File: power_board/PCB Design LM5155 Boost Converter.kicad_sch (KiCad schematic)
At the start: 62 parts, among them Q1 BSC035N04LS G, U1 LM5155_DSSR

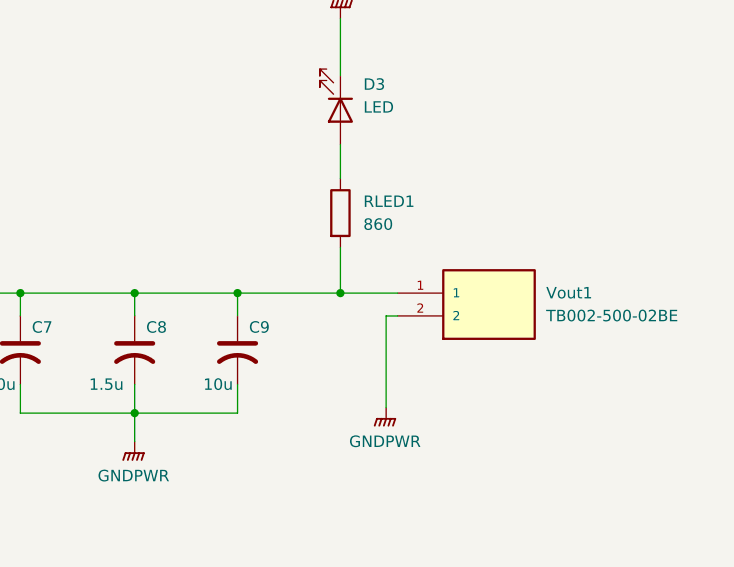
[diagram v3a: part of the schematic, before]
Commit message: Routing for TPS Module
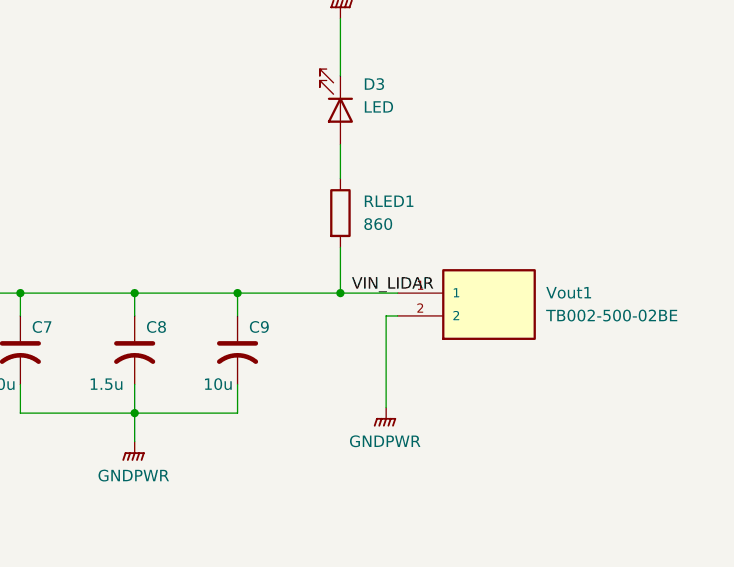
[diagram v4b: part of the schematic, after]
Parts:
- C18, C19, C21, C29: footprint (none) -> Capacitor_SMD:C_0805_2012Metric_Pad1.18x1.45mm_HandSolder
- C20, C28: footprint (none) -> Capacitor_SMD:C_1206_3216Metric_Pad1.33x1.80mm_HandSolder
- C22, C23, C30: footprint (none) -> Capacitor_SMD:C_0402_1005Metric_Pad0.74x0.62mm_HandSolder
- C24, C25: footprint (none) -> Capacitor_SMD:C_0201_0603Metric_Pad0.64x0.40mm_HandSolder
- C26, C27: footprint (none) -> Capacitor_SMD:C_0603_1608Metric_Pad1.08x0.95mm_HandSolder
- D4: footprint (none) -> Diode_SMD:D_SOD-123
- D5: footprint (none) -> LED_SMD:LED_0805_2012Metric_Pad1.15x1.40mm_HandSolder
- L2: footprint (none) -> Inductor_SMD:L_Vishay_IHLP-4040
- R10, R15, R9: footprint (none) -> Resistor_SMD:R_0603_1608Metric_Pad0.98x0.95mm_HandSolder
- R11, R12, R13, R14, R16, R17, R18, R19: footprint (none) -> Resistor_SMD:R_0402_1005Metric_Pad0.72x0.64mm_HandSolder
- TPS1: footprint (none) -> TPS552892RYQR:CONV_TPS552892RYQR
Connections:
- net VIN_LIDAR is gone; now on net COUT: C18.1, C19.1, C20.1, R18.1, TPS1.7 (VIN)
- net GND: no longer C18.2
- net PGND: now also C18.2
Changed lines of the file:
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@@
 		)
 	)
+	(label "VIN_LIDAR"
+		(at 427.99 49.53 0)
+		(effects
+			(font
+				(size 1.27 1.27)
+			)
+			(justify left bottom)
+		)
+	)
 	(label "RSENSE"
 		(at 228.6 129.54 0)
@@
 			)
 		)
-		(property "Footprint" ""
+		(property "Footprint" "Resistor_SMD:R_0402_1005Metric_Pad0.72x0.64mm_HandSolder"
 			(at 168.91 231.648 90)
 			(hide yes)
@@
 			)
 		)
-		(property "Footprint" ""
+		(property "Footprint" "Capacitor_SMD:C_0805_2012Metric_Pad1.18x1.45mm_HandSolder"
 			(at 104.14 240.3348 0)
 			(hide yes)
@@
 			)
 		)
-		(property "Footprint" ""
+		(property "Footprint" "Capacitor_SMD:C_0402_1005Metric_Pad0.74x0.62mm_HandSolder"
 			(at 143.2052 227.33 0)
 			(hide yes)
@@
 			)
 		)
-		(property "Footprint" ""
+		(property "Footprint" "Inductor_SMD:L_Vishay_IHLP-4040"
 			(at 134.62 213.36 0)
 			(hide yes)
@@
 			)
 		)
-		(property "Footprint" ""
+		(property "Footprint" "Resistor_SMD:R_0402_1005Metric_Pad0.72x0.64mm_HandSolder"
 			(at 174.752 262.89 90)
 			(hide yes)
@@
 	)
 	(symbol
-		(lib_id "power:GNDPWR")
-		(at 91.44 243.84 0)
-		(unit 1)
-		(body_style 1)
-		(exclude_from_sim no)
-		(in_bom yes)
-		(on_board yes)
-		(in_pos_files yes)
-		(dnp no)
-		(fields_autoplaced yes)
-		(property "Reference" "#PWR019"
-			(at 91.44 248.92 0)
-			(hide yes)
-			(show_name no)
-			(do_not_autoplace no)
-			(effects
-				(font
-					(size 1.27 1.27)
-				)
-			)
-		)
-		(property "Value" "GNDPWR"
-			(at 91.313 247.65 0)
-			(hide yes)
-			(show_name no)
-			(do_not_autoplace no)
-			(effects
-				(font
-					(size 1.27 1.27)
-				)
-			)
-		)
-		(property "Footprint" ""
-			(at 91.44 245.11 0)
-			(hide yes)
-			(show_name no)
-			(do_not_autoplace no)
-			(effects
-				(font
-					(size 1.27 1.27)
-				)
-			)
-		)
-		(property "Datasheet" ""
-			(at 91.44 245.11 0)
-			(hide yes)
-			(show_name no)
-			(do_not_autoplace no)
-			(effects
-				(font
-					(size 1.27 1.27)
-				)
-			)
-		)
-		(property "Description" "Power symbol creates a global label with name \"GNDPWR\" , global ground"
-			(at 91.44 243.84 0)
-			(hide yes)
-			(show_name no)
-			(do_not_autoplace no)
-			(effects
-				(font
-					(size 1.27 1.27)
-				)
-			)
-		)
-		(pin "1"
-		)
-		(instances
-			(project "PCB Design LM5155 Boost Converter"
-				(path "/085c1d8f-d12d-46a1-b7b5-945f7ea1ec15"
-					(reference "#PWR019")
-					(unit 1)
-				)
-			)
-		)
-	)
-	(symbol
 		(lib_id "power:GND")
 		(at 300.99 93.98 0)
@@
 			)
 		)
-		(property "Footprint" ""
+		(property "Footprint" "Capacitor_SMD:C_0603_1608Metric_Pad1.08x0.95mm_HandSolder"
 			(at 177.4952 274.32 0)
 			(hide yes)
@@
 			)
 		)
-		(property "Footprint" ""
+		(property "Footprint" "Capacitor_SMD:C_0805_2012Metric_Pad1.18x1.45mm_HandSolder"
 			(at 164.7952 243.84 0)
 			(hide yes)
@@
 			)
 		)
-		(property "Footprint" ""
+		(property "Footprint" "Capacitor_SMD:C_0201_0603Metric_Pad0.64x0.40mm_HandSolder"
 			(at 97.4852 262.89 0)
 			(hide yes)
@@
 			)
 		)
-		(property "Footprint" ""
+		(property "Footprint" "Capacitor_SMD:C_0805_2012Metric_Pad1.18x1.45mm_HandSolder"
 			(at 84.7852 243.84 0)
 			(hide yes)
@@
 			)
 		)
-		(property "Footprint" ""
+		(property "Footprint" "Capacitor_SMD:C_0402_1005Metric_Pad0.74x0.62mm_HandSolder"
 			(at 127.9652 227.33 0)
 			(hide yes)
@@
 			)
 		)
-		(property "Footprint" ""
+		(property "Footprint" "Resistor_SMD:R_0603_1608Metric_Pad0.98x0.95mm_HandSolder"
 			(at 187.452 243.84 90)
 			(hide yes)
@@
 			)
 		)
-		(property "Footprint" ""
+		(property "Footprint" "Capacitor_SMD:C_0402_1005Metric_Pad0.74x0.62mm_HandSolder"
 			(at 180.34 246.6848 0)
 			(hide yes)
@@
 			)
 		)
-		(property "Footprint" ""
+		(property "Footprint" "LED_SMD:LED_0805_2012Metric_Pad1.15x1.40mm_HandSolder"
 			(at 176.53 229.87 0)
 			(hide yes)
@@
 			)
 		)
-		(property "Footprint" ""
+		(property "Footprint" "Capacitor_SMD:C_1206_3216Metric_Pad1.33x1.80mm_HandSolder"
 			(at 77.1652 243.84 0)
 			(hide yes)
@@
 			)
 		)
-		(property "Footprint" ""
+		(property "Footprint" "Resistor_SMD:R_0402_1005Metric_Pad0.72x0.64mm_HandSolder"
 			(at 103.632 260.35 90)
 			(hide yes)
@@
 			)
 		)
-		(property "Footprint" ""
+		(property "Footprint" "Diode_SMD:D_SOD-123"
 			(at 68.58 257.81 0)
 			(hide yes)
@@
 			)
 		)
-		(property "Footprint" ""
+		(property "Footprint" "Resistor_SMD:R_0402_1005Metric_Pad0.72x0.64mm_HandSolder"
 			(at 198.882 243.84 90)
 			(hide yes)
@@
 			)
 		)
-		(property "Footprint" ""
+		(property "Footprint" "Resistor_SMD:R_0402_1005Metric_Pad0.72x0.64mm_HandSolder"
 			(at 153.162 269.24 90)
 			(hide yes)
@@
 			)
 		)
-		(property "Footprint" ""
+		(property "Footprint" "TPS552892RYQR:CONV_TPS552892RYQR"
 			(at 119.38 236.22 0)
 			(hide yes)
@@
 			)
 		)
-		(property "Footprint" ""
+		(property "Footprint" "Resistor_SMD:R_0402_1005Metric_Pad0.72x0.64mm_HandSolder"
 			(at 66.802 243.84 90)
 			(hide yes)
@@
 			)
 		)
-		(property "Footprint" ""
+		(property "Footprint" "Capacitor_SMD:C_1206_3216Metric_Pad1.33x1.80mm_HandSolder"
 			(at 158.4452 243.84 0)
 			(hide yes)
@@
 			)
 		)
-		(property "Footprint" ""
+		(property "Footprint" "Resistor_SMD:R_0402_1005Metric_Pad0.72x0.64mm_HandSolder"
 			(at 176.53 237.998 90)
 			(hide yes)
@@
 			)
 		)
-		(property "Footprint" ""
+		(property "Footprint" "Resistor_SMD:R_0603_1608Metric_Pad0.98x0.95mm_HandSolder"
 			(at 110.49 248.158 90)
 			(hide yes)
@@
 			)
 		)
-		(property "Footprint" ""
+		(property "Footprint" "Resistor_SMD:R_0402_1005Metric_Pad0.72x0.64mm_HandSolder"
 			(at 187.452 262.89 90)
 			(hide yes)
@@
 	)
 	(symbol
+		(lib_id "power:GNDPWR")
+		(at 91.44 243.84 0)
+		(unit 1)
+		(body_style 1)
+		(exclude_from_sim no)
+		(in_bom yes)
+		(on_board yes)
+		(in_pos_files yes)
+		(dnp no)
+		(fields_autoplaced yes)
+		(property "Reference" "#PWR019"
+			(at 91.44 248.92 0)
+			(hide yes)
+			(show_name no)
+			(do_not_autoplace no)
+			(effects
+				(font
+					(size 1.27 1.27)
+				)
+			)
+		)
+		(property "Value" "PGND"
+			(at 91.313 247.65 0)
+			(hide yes)
+			(show_name no)
+			(do_not_autoplace no)
+			(effects
+				(font
+					(size 1.27 1.27)
+				)
+			)
+		)
+		(property "Footprint" ""
+			(at 91.44 245.11 0)
+			(hide yes)
+			(show_name no)
+			(do_not_autoplace no)
+			(effects
+				(font
+					(size 1.27 1.27)
+				)
+			)
+		)
+		(property "Datasheet" ""
+			(at 91.44 245.11 0)
+			(hide yes)
+			(show_name no)
+			(do_not_autoplace no)
+			(effects
+				(font
+					(size 1.27 1.27)
+				)
+			)
+		)
+		(property "Description" "Power symbol creates a global label with name \"GNDPWR\" , global ground"
+			(at 91.44 243.84 0)
+			(hide yes)
+			(show_name no)
+			(do_not_autoplace no)
+			(effects
+				(font
+					(size 1.27 1.27)
+				)
+			)
+		)
+		(pin "1"
+		)
+		(instances
+			(project "PCB Design LM5155 Boost Converter"
+				(path "/085c1d8f-d12d-46a1-b7b5-945f7ea1ec15"
+					(reference "#PWR019")
+					(unit 1)
+				)
+			)
+		)
+	)
+	(symbol
 		(lib_id "Device:C_Polarized_US")
 		(at 356.87 55.88 0)
@@
 			)
 		)
-		(property "Footprint" ""
+		(property "Footprint" "Resistor_SMD:R_0603_1608Metric_Pad0.98x0.95mm_HandSolder"
 			(at 110.49 242.062 90)
 			(hide yes)
@@
 			)
 		)
-		(property "Footprint" ""
+		(property "Footprint" "Capacitor_SMD:C_0201_0603Metric_Pad0.64x0.40mm_HandSolder"
 			(at 89.8652 262.89 0)
 			(hide yes)
@@
 			)
 		)
-		(property "Footprint" ""
+		(property "Footprint" "Capacitor_SMD:C_0603_1608Metric_Pad1.08x0.95mm_HandSolder"
 			(at 167.3352 271.78 0)
 			(hide yes)
@@
 			)
 		)
-		(property "Footprint" ""
+		(property "Footprint" "Capacitor_SMD:C_0805_2012Metric_Pad1.18x1.45mm_HandSolder"
 			(at 92.4052 243.84 0)
 			(hide yes)
